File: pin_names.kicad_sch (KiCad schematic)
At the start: 1 part

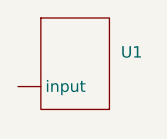
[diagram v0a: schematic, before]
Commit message: adding pin number
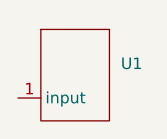
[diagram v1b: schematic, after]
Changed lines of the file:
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@@
 	(symbol
 		(lib_id "custom_lib:pin_name_test")
-		(at 31.75 29.21 0)
+		(at 31.75 30.48 0)
 		(unit 1)
 		(exclude_from_sim no)
@@
 		(fields_autoplaced yes)
 		(property "Reference" "U1"
-			(at 36.83 29.2099 0)
+			(at 36.83 30.4799 0)
 			(effects
 				(font
@@
 		)
 		(property "Value" "~"
-			(at 36.83 31.7499 0)
+			(at 36.83 33.0199 0)
 			(effects
 				(font
@@
 		)
 		(property "Footprint" ""
-			(at 31.75 29.21 0)
+			(at 31.75 30.48 0)
 			(effects
 				(font
@@
 		)
 		(property "Datasheet" ""
-			(at 31.75 29.21 0)
+			(at 31.75 30.48 0)
 			(effects
 				(font
@@
 		)
 		(property "Description" ""
-			(at 31.75 29.21 0)
+			(at 31.75 30.48 0)
 			(effects
 				(font
@@
 			)
 		)
-		(pin ""
+		(pin "1"
 		)
 		(instances
